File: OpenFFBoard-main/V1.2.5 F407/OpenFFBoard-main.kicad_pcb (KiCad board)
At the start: 2 copper layers, 60 x 60 mm, 66 parts, among them J1 USB4105-GF-A, SW1 TL3342F160QG, SW2 TL3342F160QG, U1 STM32F407VGT6, U2 TJA1051T-3, U3 LM1117-3.3, U4 USBLC6-2SC6, X1 8MHz

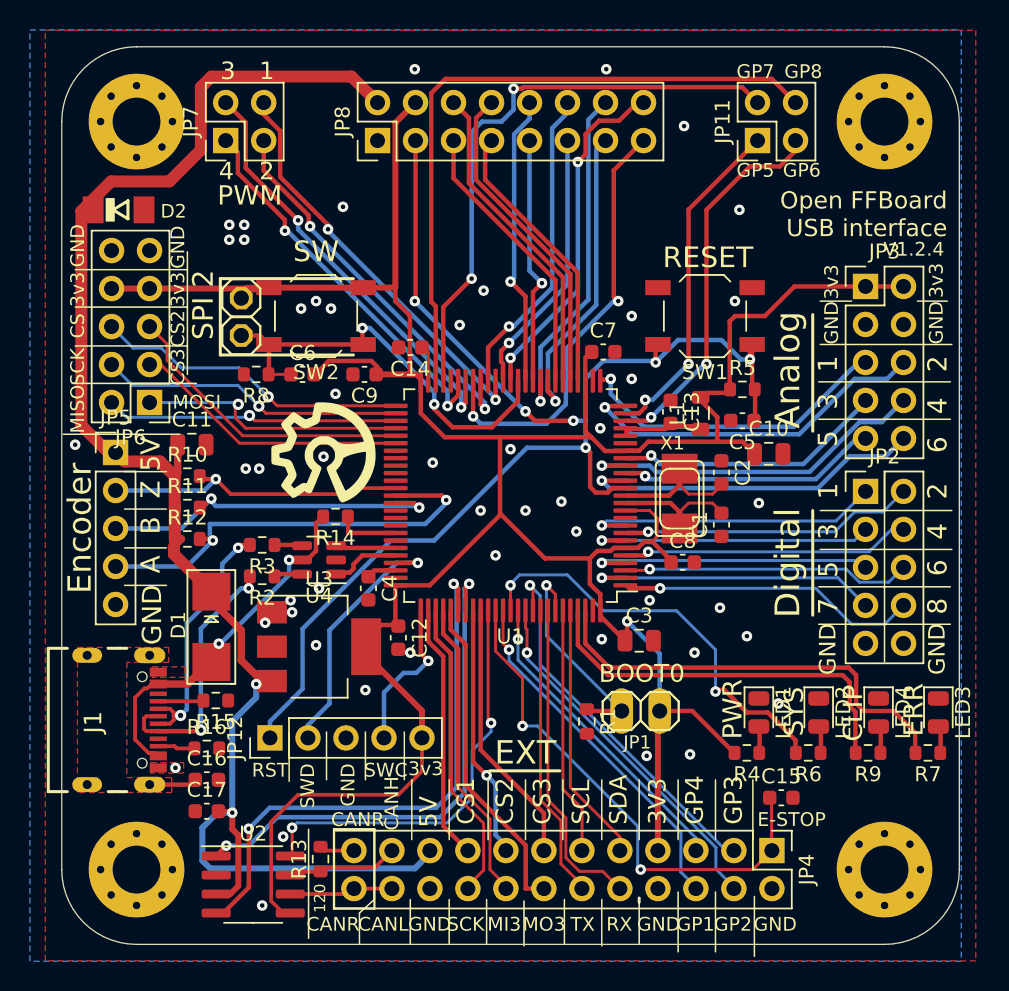
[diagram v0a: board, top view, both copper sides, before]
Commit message: defined net class rules and added missing 3d models
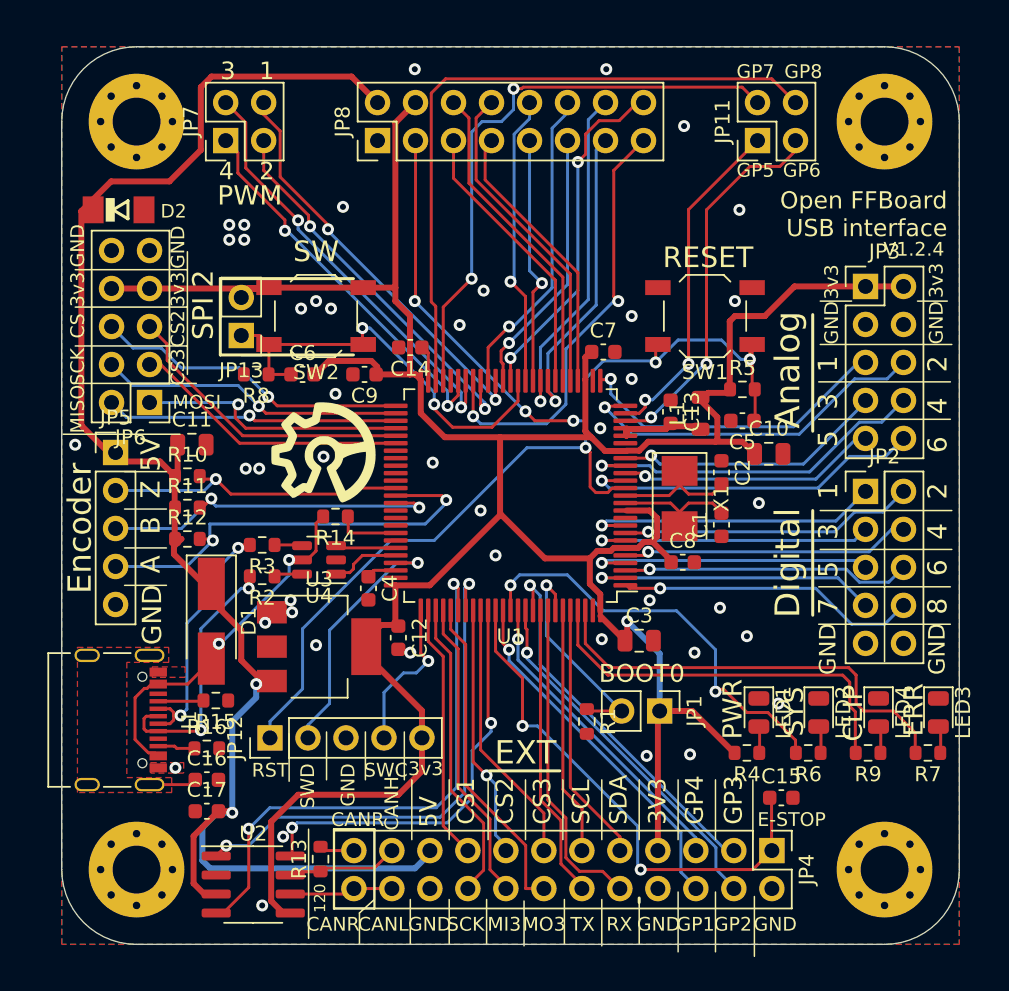
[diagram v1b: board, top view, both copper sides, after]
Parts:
- removed JP14: PINHD-1X1, stm_board_f407_1.2.4:1X01
- D1: value LV HC low drop -> MMD SS14; footprint stm_board_f407_1.2.4:SMADIODE -> Diode_SMD:D_SMA_Handsoldering
- J1: footprint stm_board_f407_1.2.4:GCT_USB4105-GF-A -> Connector_USB:USB_C_Receptacle_Palconn_UTC16-G
- JP1: footprint stm_board_f407_1.2.4:1X02 -> Connector_PinHeader_2.54mm:PinHeader_1x02_P2.54mm_Vertical
- JP13: value PINHD-1X1 -> Button A; footprint stm_board_f407_1.2.4:1X01 -> Connector_PinHeader_2.54mm:PinHeader_1x02_P2.54mm_Vertical
- X1: footprint stm_board_f407_1.2.4:NX5032 -> Crystal:Crystal_SMD_5032-2Pin_5.0x3.2mm
- moved JP13 2.50 mm to (130.5, 94.3), turned to 180 degrees
- moved J1 2.24 mm to (122.4, 120.0)
- moved JP1 1.27 mm to (158.5, 119.4), turned to -90 degrees
- moved D1 0.37 mm to (128.5, 113.4)
- turned X1 to -90 degrees
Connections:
- JP13 pad 1: +3.3V -> /BUTTON_A
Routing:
- net +5V: track 108.3 -> 104.6 mm, vias 3 -> 2
- net +3.3V: track 201.4 -> 198.3 mm, vias 5 -> 1
- net /USB_VBUS_IN: track 25.2 -> 22.9 mm
- net /NRST: track 87.9 -> 87.2 mm
- net /BRAKE_CTRL: track 20.9 -> 20.2 mm
- net /GPIO6: track 25.5 -> 24.8 mm
- net /DIN4: track 19.5 -> 18.9 mm
- net /CAN_RX: track 37.7 -> 37.0 mm
- net /SPI1_SS1: track 18.7 -> 18.1 mm
- net /AIN4: track 17.3 -> 16.7 mm
- net /GPIO3: track 25.5 -> 25.0 mm
- net /CANH: track 7.30 -> 6.94 mm, vias 1 -> 0
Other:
- copper layers 2 -> 4
